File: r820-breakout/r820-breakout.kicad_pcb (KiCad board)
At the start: 2 copper layers, 30.5 x 54.6 mm, 18 parts, among them J1 Conn_Coaxial, J2 Conn_01x10, J3 Conn_01x02, J4 Conn_01x02, U1 R820T, Y1 16MHz CL=16pF

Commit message: Heavily reworked.
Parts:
- removed J3: Conn_01x02, Connector_PinHeader_2.54mm:PinHeader_1x02_P2.54mm_Vertical
- added C10: C, Capacitors_SMD:C_0402, F.Cu at (120.8, 105.1)
- added C11: C, Capacitors_SMD:C_0402, F.Cu at (122.2, 105.1)
- added C12: 330p, Capacitors_SMD:C_0603, F.Cu at (107.8, 85.8)
- added C13: 10n, Capacitors_SMD:C_0603, F.Cu at (107.8, 79.2)
- added C14: 100n, Capacitors_SMD:C_0603, F.Cu at (113.9, 77.6)
- added C15: 100nF, Capacitors_SMD:C_0402, F.Cu at (109.5, 94.7)
- added C16: 100nF, Capacitors_SMD:C_0402, F.Cu at (114.8, 99.1)
- added D1: BAV99, TO_SOT_Packages_SMD:SOT-23, F.Cu at (106.6, 82.5)
- added L3: 8.2n, Inductors_SMD:L_0603, F.Cu at (107.8, 88.7)
- added L4: 180n, Inductors_SMD:L_0603, F.Cu at (110.1, 78.4)
- C1, C2, C3, C5: footprint Capacitor_SMD:C_0603_1608Metric -> Capacitors_SMD:C_0402
- J1: footprint Connector_Coaxial:SMA_Molex_73251-2200_Horizontal -> Connectors_Molex:Molex_SMA_Jack_Edge_Mount
- J4: moved to F.Cu
- U1: footprint Sensor_Motion:InvenSense_QFN-24_4x4mm_P0.5mm -> Housings_DFN_QFN:QFN-24-1EP_4x4mm_Pitch0.5mm
- Y1: value 16MHz CL=16pF -> Crystal_GND24; footprint Crystal:Crystal_HC49-4H_Vertical -> Crystals:Crystal_SMD_TXC_7M-4pin_3.2x2.5mm
- moved C7 10.4 mm to (107.6, 102.6), turned to 90 degrees
- moved C6 10.1 mm to (113.8, 102.6)
- moved J4 8.07 mm to (116.9, 78.4), turned to 90 degrees
- moved J2 7.83 mm to (102.5, 111.6)
- moved C1 7.05 mm to (116.4, 93.3), turned to 270 degrees
- moved C2 6.59 mm to (111.6, 91.5), turned to 0 degrees
- moved Y1 6.19 mm to (110.7, 102.6)
- moved J1 5.30 mm to (107.8, 73.0), turned to 270 degrees
- moved L1 2.74 mm to (112.7, 87.7), turned to 270 degrees
- moved L2 2.71 mm to (115.0, 87.7)
- moved C4 2.32 mm to (105.2, 94.8)
- moved C5 1.85 mm to (105.2, 96.0)
- moved C8 0.94 mm to (125.3, 94.8)
- moved C3 0.90 mm to (122.4, 94.0)
- moved C9 0.90 mm to (122.4, 95.9)
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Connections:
- J2 pad 2: VDD_3V -> GND
- J2 pad 3: GND -> T_SCL
- J2 pad 4: GND -> T_SDA
- J2 pad 5: T_SDA -> GND
- J2 pad 6: T_SCL -> T_CLK_Out
- J2 pad 7: T_CLK_Out -> GND
- J4 pad 1: GND -> Net-(C14-Pad2)
- U1 pad 1: (no net) -> Net-(U1-Pad1)
- U1 pad 12: T_IF_N -> Net-(C10-Pad1)
- U1 pad 13: T_IF_P -> Net-(C11-Pad1)
- U1 pad 24: T_RF_IN -> Net-(L3-Pad2)
- U1 pad 3: (no net) -> Net-(U1-Pad3)
- Y1 pad 2: Net-(C7-Pad1) -> GND
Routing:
- net GND: track 110.8 -> 25.7 mm, vias 3 -> 86
- net VDD_3V: track 112.6 -> 50.8 mm, vias 6 -> 4
- net T_IF_P: track 28.6 -> 6.01 mm
- net T_IF_N: track 26.2 -> 5.97 mm
- net T_RF_IN: track 23.8 -> 8.74 mm
- net Net-(C11-Pad1): track 0.00 -> 10.8 mm
- net T_IF_AGC: track 31.2 -> 20.5 mm
- net Net-(C10-Pad1): track 0.00 -> 10.0 mm
- net T_CLK_Out: track 24.5 -> 15.1 mm
- net Net-(C6-Pad1): track 15.7 -> 6.54 mm
- net T_SCL: track 28.1 -> 19.1 mm, vias 2 -> 0
- net Net-(L1-Pad2): track 12.9 -> 4.87 mm
- net Net-(L3-Pad2): track 0.00 -> 6.43 mm
- net Net-(C14-Pad2): track 0.00 -> 6.09 mm
- net Net-(L2-Pad2): track 13.0 -> 7.08 mm, vias 2 -> 0
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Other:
- board size 30.5 x 54.6 mm -> 28 x 45 mm
- net class Default: clearance 0.2 -> 0.15
- rule trace_clearance: 0.2 -> 0.15
- rule trace_min: 0.2 -> 0.15
- board text added: "R820T breakout board Original by @siddolo, modded by @hennichodernich"
- board text removed: "R820 breakout board https://github.com/siddolo"

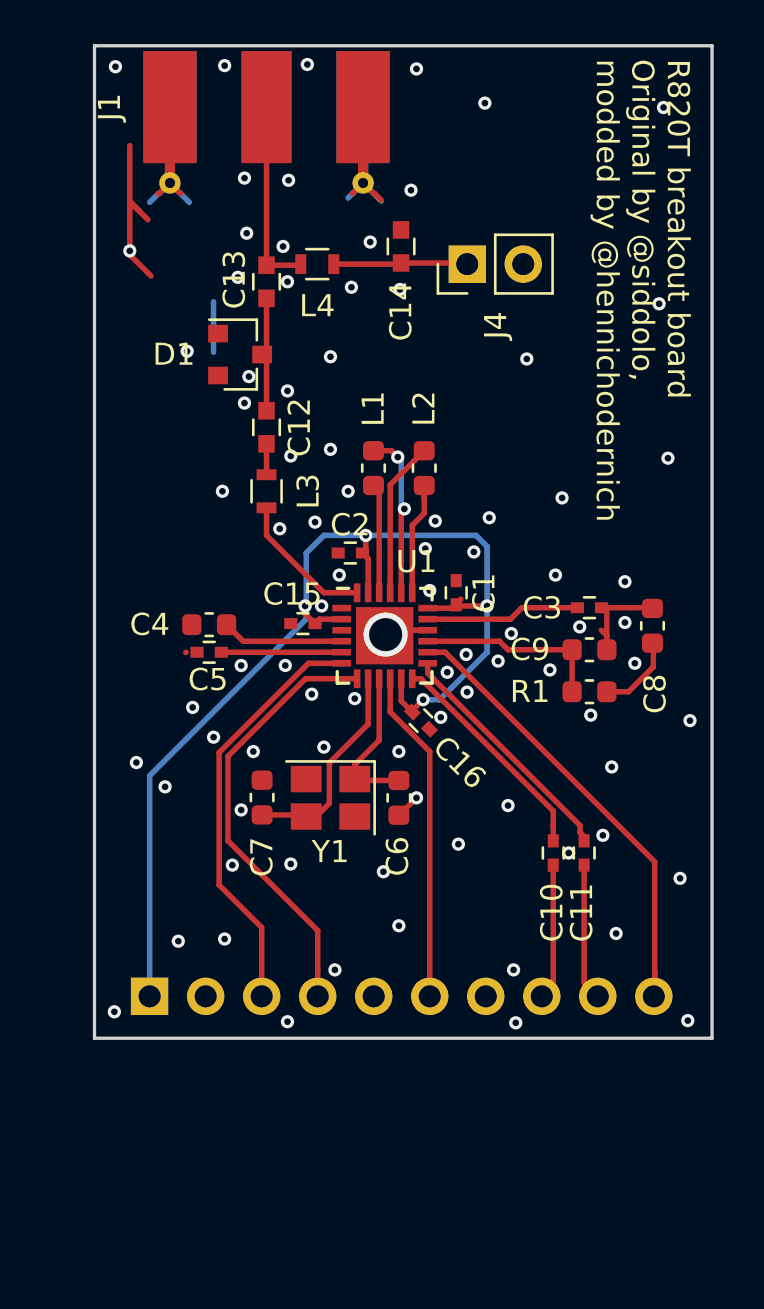
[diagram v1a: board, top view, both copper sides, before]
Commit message: footprint fix, added OSH logo, removed big via under rt820t
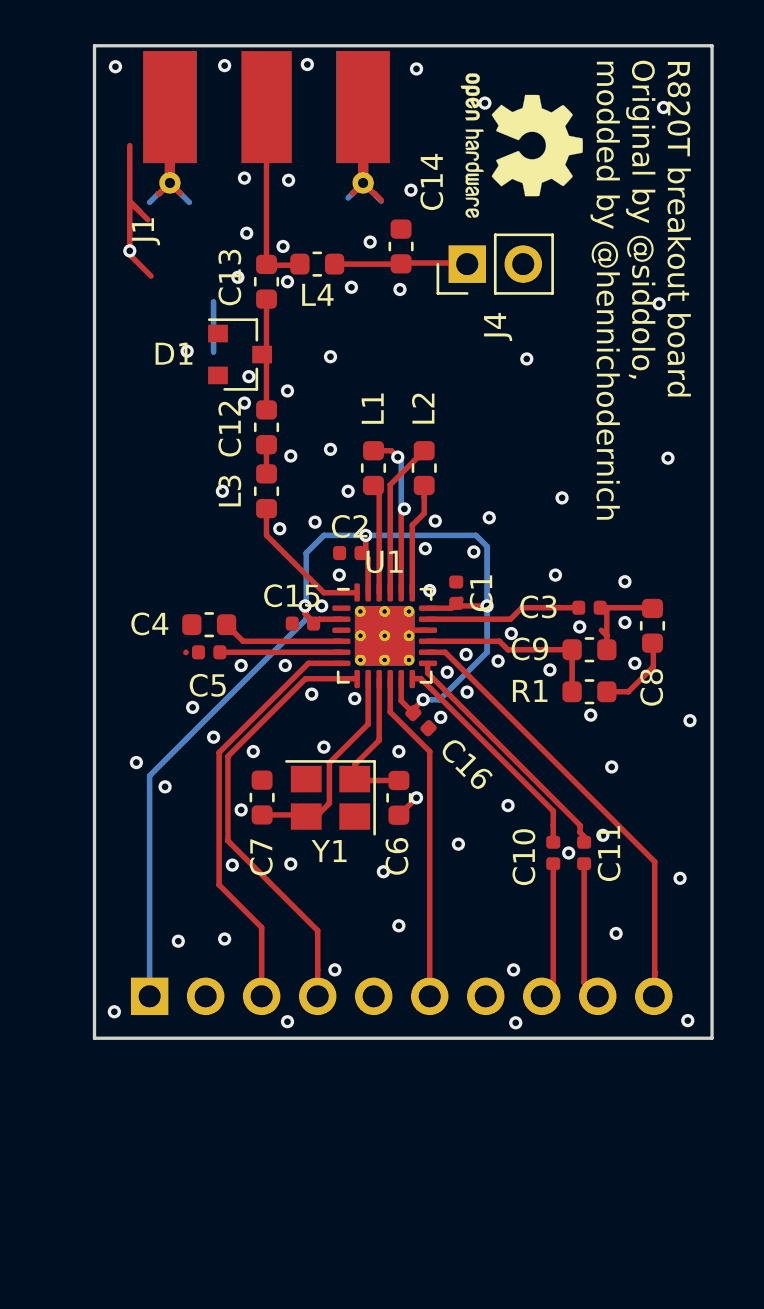
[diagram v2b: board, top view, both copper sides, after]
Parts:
- added REF**: OSHW-Logo2_7.3x6mm_SilkScreen, Symbol:OSHW-Logo2_7.3x6mm_SilkScreen, F.Cu at (119.4, 73.0)
- C1, C10, C11, C15, C16, C2, C3, C5: footprint Capacitors_SMD:C_0402 -> Capacitor_SMD:C_0402_1005Metric
- C12, C13, C14: footprint Capacitors_SMD:C_0603 -> Capacitor_SMD:C_0603_1608Metric
- D1: footprint TO_SOT_Packages_SMD:SOT-23 -> Package_TO_SOT_SMD:SOT-23
- L3, L4: footprint Inductors_SMD:L_0603 -> Inductor_SMD:L_0603_1608Metric
- U1: footprint Housings_DFN_QFN:QFN-24-1EP_4x4mm_Pitch0.5mm -> Package_DFN_QFN:QFN-24-1EP_4x4mm_P0.5mm_EP2.7x2.7mm_ThermalVias
- Y1: footprint Crystals:Crystal_SMD_TXC_7M-4pin_3.2x2.5mm -> Crystal:Crystal_SMD_TXC_7M-4Pin_3.2x2.5mm
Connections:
- U1 pad 1: Net-(U1-Pad1) -> (no net)
- U1 pad 3: Net-(U1-Pad3) -> (no net)
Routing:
- net GND: vias 86 -> 85

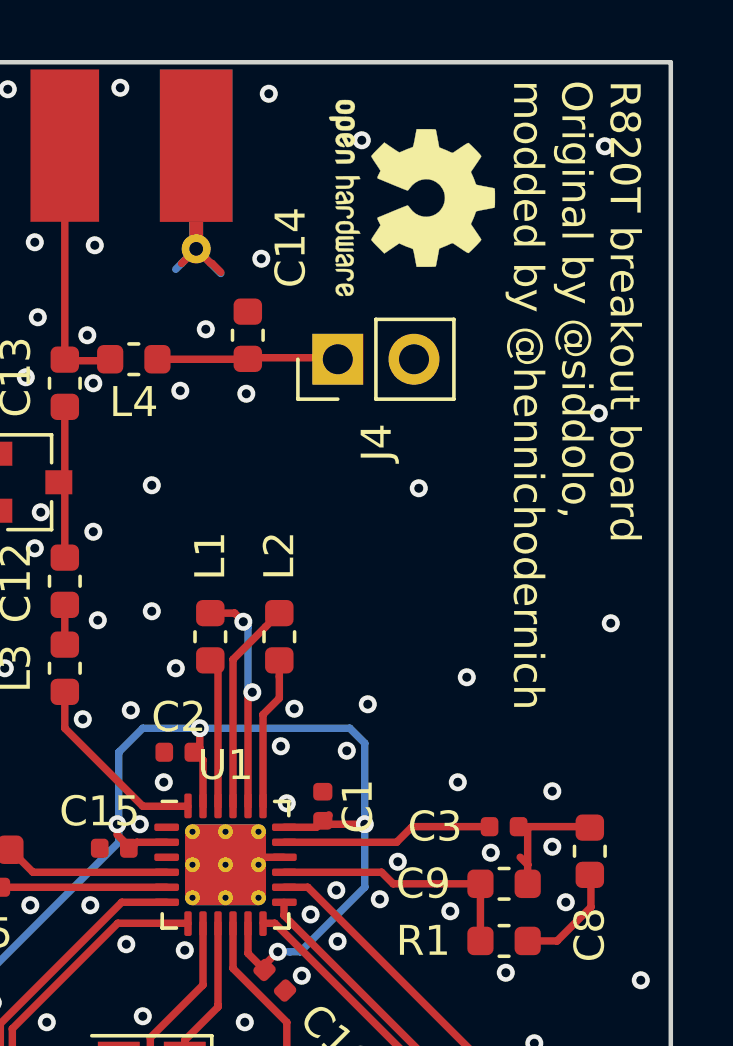
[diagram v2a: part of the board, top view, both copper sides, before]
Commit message: Fix F.Cu fill zone clearance
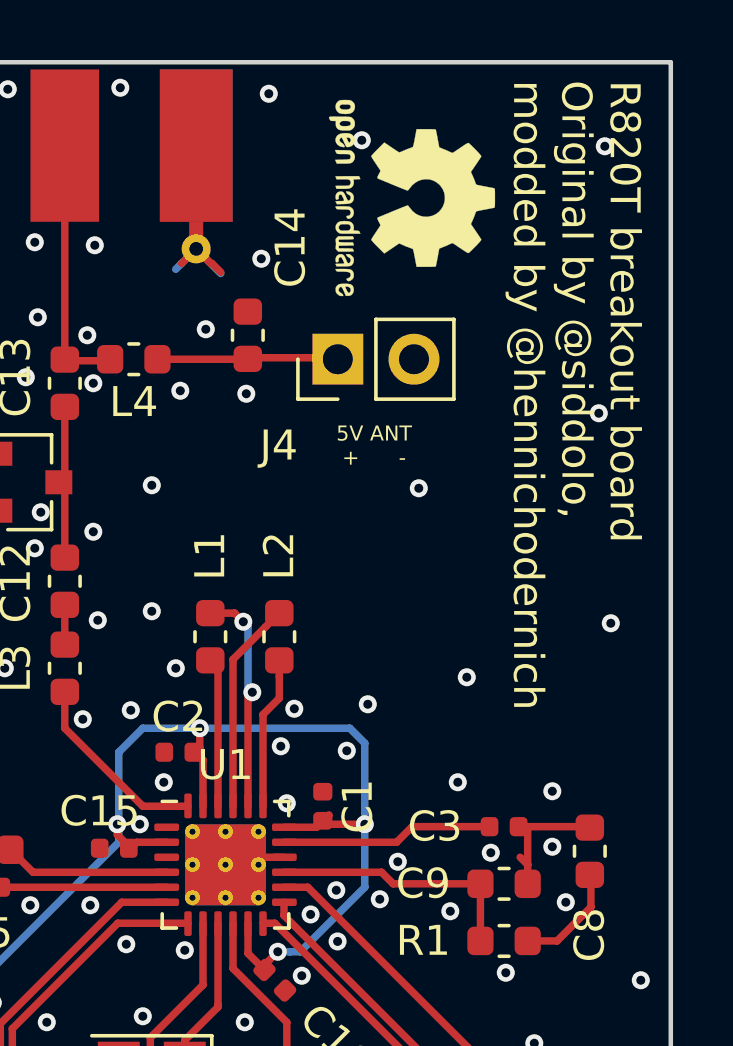
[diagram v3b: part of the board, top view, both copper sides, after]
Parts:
- C10, C11: value C -> 100nF
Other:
- board text added: "5V ANT + -"
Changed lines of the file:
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@@
   (general
     (thickness 1.6)
-    (drawings 5)
+    (drawings 6)
     (tracks 243)
     (zones 0)
@@
   )
   (layers
-    (0 F.Cu signal)
-    (31 B.Cu signal)
+    (0 F.Cu signal hide)
+    (31 B.Cu signal hide)
     (32 B.Adhes user)
     (33 F.Adhes user)
@@
     (visible_elements FFFFFF7F)
     (pcbplotparams
-      (layerselection 0x010fc_ffffffff)
+      (layerselection 0x010f0_ffffffff)
       (usegerberextensions false)
-      (usegerberattributes false)
+      (usegerberattributes true)
       (usegerberadvancedattributes false)
       (creategerberjobfile false)
@@
       (viasonmask false)
       (mode 1)
-      (useauxorigin false)
+      (useauxorigin true)
       (hpglpennumber 1)
       (hpglpenspeed 20)
@@
       (drillshape 0)
       (scaleselection 1)
-      (outputdirectory "./"))
+      (outputdirectory "../test/"))
   )
   (net 0 "")
@@
     (descr "Through hole straight pin header, 1x02, 2.54mm pitch, single row")
     (tags "Through hole pin header THT 1x02 2.54mm single row")
-    (fp_text reference J4 (at -2.775 1.3 90) (layer F.SilkS)
+    (fp_text reference J4 (at -2.88 -1.965 180) (layer F.SilkS)
       (effects (font (size 1 1) (thickness 0.15)))
     )
@@
       (effects (font (size 1 1) (thickness 0.15)))
     )
-    (fp_text value C (at 0 1.17 270) (layer F.Fab)
+    (fp_text value 100nF (at 0 1.17 270) (layer F.Fab)
       (effects (font (size 1 1) (thickness 0.15)))
     )
@@
       (effects (font (size 1 1) (thickness 0.15)))
     )
-    (fp_text value C (at 0 1.17 270) (layer F.Fab)
+    (fp_text value 100nF (at 0 1.17 270) (layer F.Fab)
       (effects (font (size 1 1) (thickness 0.15)))
     )
@@
       (xy -2.549664 1.91989) (xy -2.469928 1.911165) (xy -2.400256 1.919918)) (layer F.SilkS) (width 0.01))
   )
+  (gr_text "5V ANT\n+      -" (at 118.11 81.28) (layer F.SilkS)
+    (effects (font (size 0.5 0.5) (thickness 0.125)))
+  )
   (gr_text "R820T breakout board\nOriginal by @siddolo, \nmodded by @hennichodernich" (at 124.85 69.1 270) (layer F.SilkS)
-    (effects (font (size 1 1) (thickness 0.25)) (justify left))
+    (effects (font (size 1 1) (thickness 0.15)) (justify left))
   )
   (gr_line (start 100 113.5) (end 100 68.5) (layer Edge.Cuts) (width 0.15))
